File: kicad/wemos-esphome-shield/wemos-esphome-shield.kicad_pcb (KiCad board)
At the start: 2 copper layers, 74 x 54 mm, 13 parts, among them Q1 2N2219, T1 Transformer_1P_1S, U1 WeMos_D1_mini

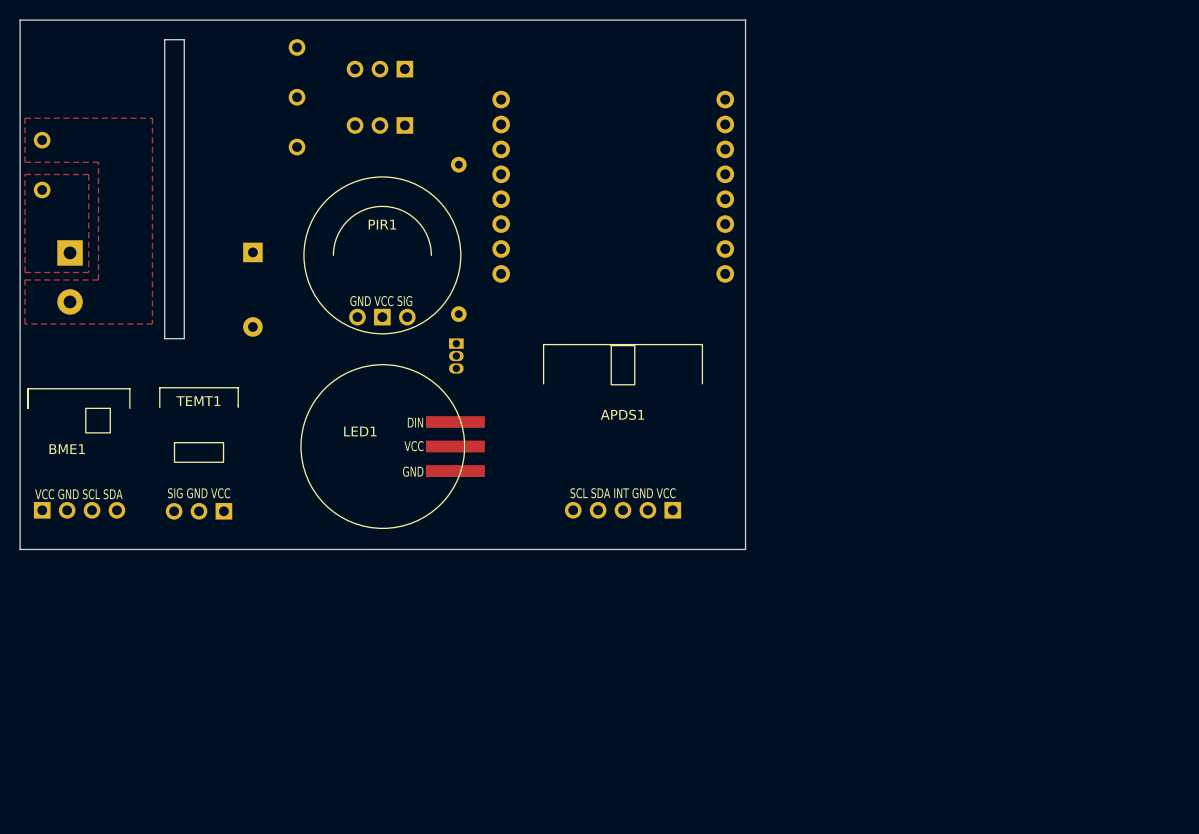
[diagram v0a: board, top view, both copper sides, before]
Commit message: Fix some electrical net, new cut edge, new netclasses
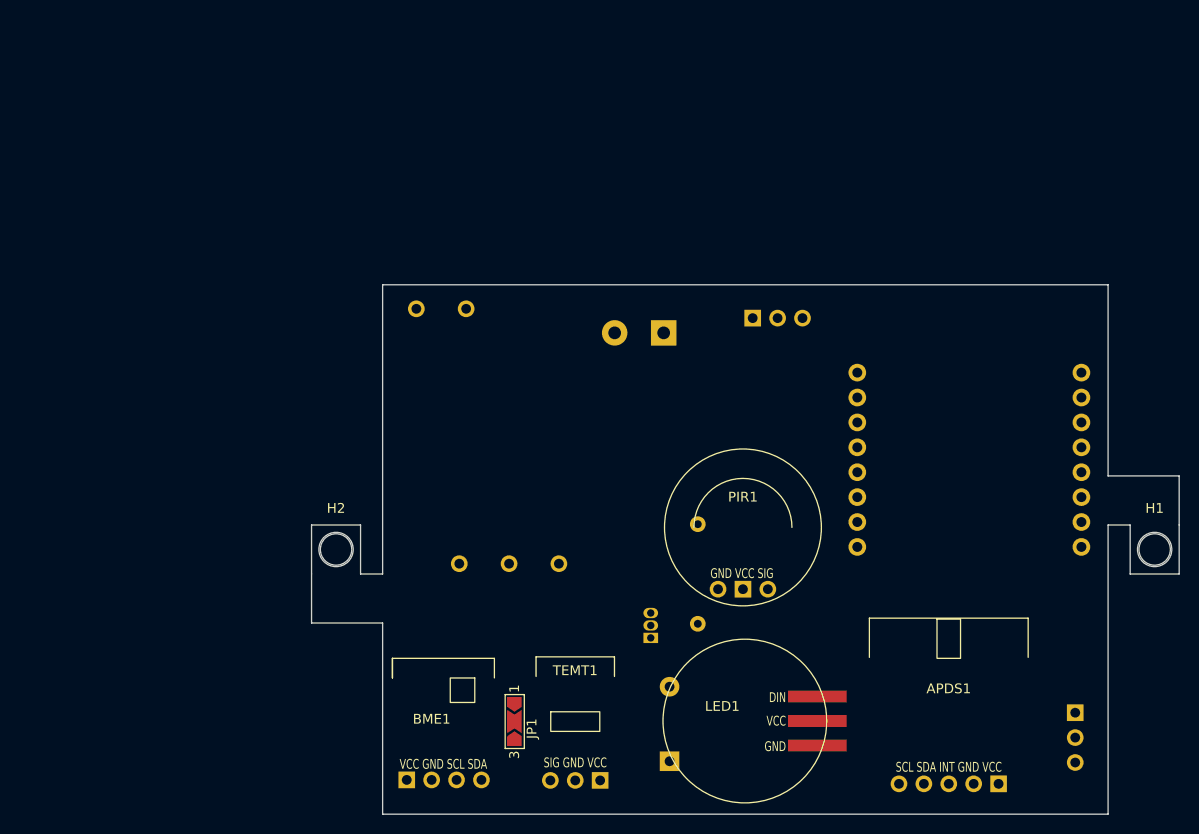
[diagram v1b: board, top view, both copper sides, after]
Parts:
- added H1: MountingHole, MountingHole:MountingHole_3.2mm_M3, F.Cu at (157.7, 91.0)
- added H2: MountingHole, MountingHole:MountingHole_3.2mm_M3, F.Cu at (74.2, 91.0)
- added JP1: SolderJumper_3_Open, Jumper:SolderJumper-3_P2.0mm_Open_TrianglePad1.0x1.5mm_NumberLabels, F.Cu at (92.4, 108.5)
- APDS1: value Conn_01x04_Female -> Conn_01x05_Female
- R1: footprint Resistor_THT:R_Axial_DIN0207_L6.3mm_D2.5mm_P15.24mm_Horizontal -> Resistor_THT:R_Axial_DIN0207_L6.3mm_D2.5mm_P10.16mm_Horizontal
- moved RELAY1 94.8 mm to (149.6, 107.7), turned to 180 degrees
- moved BZ1 67.1 mm to (108.2, 112.6), turned to 90 degrees
- moved POWER1 61.1 mm to (107.7, 68.9), turned to 180 degrees
- moved TEMT1 47.2 mm to (98.6, 114.6)
- moved LED1 46.3 mm to (115.9, 108.5)
- moved BME1 46.2 mm to (84.0, 114.5)
- moved PIR1 46.1 mm to (115.7, 95.0)
- moved U1 45.8 mm to (138.8, 81.8)
- moved T1 45.6 mm to (89.5, 79.5), turned to -90 degrees
- moved R1 44.0 mm to (111.1, 88.4)
- moved APDS1 43.4 mm to (136.7, 114.9)
- moved RELAY2 40.6 mm to (116.7, 67.4), turned to -90 degrees
- moved Q1 36.0 mm to (106.3, 100.0), turned to 90 degrees
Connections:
- APDS1 pad 1: SDA -> SCL
- APDS1 pad 2: SCL -> SDA
- APDS1 pad 3: 5V -> unconnected-(APDS1-Pad3)
- APDS1 pad 5: (no net) -> 5V
- BME1 pad 1: SDA -> Net-(JP1-Pad2)
- BME1 pad 2: SCL -> GND
- BME1 pad 3: 5V -> SCL
- BME1 pad 4: GND -> SDA
- PIR1 pad 1: 3.3V -> GND
- PIR1 pad 2: GND -> 3.3V
- TEMT1 pad 1: 5V -> TEMT6000
- TEMT1 pad 2: TEMT6000 -> GND
- TEMT1 pad 3: GND -> 5V
- U1 pad 9: 5V -> VCC
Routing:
- removed copper zone on F.Cu, net L
- removed copper zone on F.Cu, net N
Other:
- board size 74 x 54 mm -> 88.5 x 54 mm

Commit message: first routing version
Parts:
- moved RELAY2 49.8 mm to (144.9, 108.4), turned to 0 degrees
- moved Q1 19.0 mm to (105.8, 81.0)
- moved BZ1 14.3 mm to (106.2, 98.5)
- moved R1 13.7 mm to (102.3, 78.0)
- moved LED1 7.05 mm to (115.8, 101.5), turned to -90 degrees
- moved JP1 6.43 mm to (93.5, 102.2)
- moved TEMT1 6.27 mm to (99.5, 108.4)
- moved APDS1 6.22 mm to (134.8, 109.0)
- moved BME1 6.15 mm to (84.8, 108.4)
- moved PIR1 4.31 mm to (116.0, 90.8)
- moved U1 2.34 mm to (136.6, 81.2)
- moved RELAY1 0.81 mm to (150.0, 108.4), turned to 0 degrees
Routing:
- net GND: track 0.00 -> 189.2 mm
- net 3.3V: track 0.00 -> 99.1 mm
- net SCL: track 0.00 -> 79.0 mm
- net TEMT6000: track 0.00 -> 76.6 mm
- net SDA: track 0.00 -> 74.1 mm, vias 0 -> 1
- net 5V: track 0.00 -> 72.8 mm
- net LED: track 0.00 -> 52.3 mm, vias 0 -> 1
- net VCC: track 0.00 -> 38.8 mm
- net L: track 0.00 -> 30.2 mm
- net RELAY1: track 0.00 -> 28.8 mm
- net BUZZER: track 0.00 -> 25.7 mm
- net RELAY2: track 0.00 -> 24.7 mm
- net Net-(BZ1-Pad2): track 0.33 -> 19.4 mm
- net N: track 0.00 -> 16.2 mm
- net Net-(JP1-Pad2): track 0.14 -> 16.3 mm
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
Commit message: update APDS footprint for future compatibility
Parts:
- APDS1: footprint internal:APDS9960 -> internal:APDS9960 double pinout
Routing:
- net SCL: track 79.0 -> 91.8 mm
- net SDA: track 74.1 -> 82.0 mm
- net GND: track 189.2 -> 192.3 mm
- net 5V: track 72.8 -> 75.8 mm
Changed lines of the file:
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@@
   (net 21 "RELAY2")
   (net 22 "unconnected-(APDS1-Pad3)")
-  (net 23 "Net-(JP1-Pad2)")
+  (net 23 "Net-(BME1-Pad1)")
   (footprint "internal:SR602" locked (layer "F.Cu")
     (at 115.954688 90.75)
@@
       (net 1 "5V") (pinfunction "Pin_3") (pintype "passive"))
   )
-  (footprint "internal:APDS9960" (layer "F.Cu")
+  (footprint "internal:APDS9960 double pinout" (layer "F.Cu")
     (at 134.75 109.005)
     (property "Sheetfile" "wemos-esphome-shield.kicad_sch")
@@
       (effects (font (size 1 1) (thickness 0.15)))
     )
-    (fp_text user "SCL SDA INT GND VCC" (at 0 -1.7 unlocked) (layer "F.SilkS")
+    (fp_text user "GND VCC SDA SCL" (at 0 3.8 unlocked) (layer "F.SilkS")
+      (effects (font (size 1 0.7) (thickness 0.15)))
+    )
+    (fp_text user "SCL SDA INT GND VCC" (at 0 -1.6 unlocked) (layer "F.SilkS")
       (effects (font (size 1 0.7) (thickness 0.15)))
     )
@@
     (fp_line (start 8.1 -16.9) (end 8.1 -12.9) (layer "F.SilkS") (width 0.12))
     (fp_line (start -8.1 -16.9) (end -8.1 -12.9) (layer "F.SilkS") (width 0.12))
-    (fp_line (start -8.1 -16.9) (end 8.1 -16.9) (layer "F.SilkS") (width 0.12))
     (fp_rect (start -1.2 -16.8) (end 1.2 -12.8) (layer "F.SilkS") (width 0.12) (fill none))
-    (fp_rect (start -8.1 1.1) (end 8.1 -16.9) (layer "F.Fab") (width 0.1) (fill none))
+    (fp_rect (start -8.1 -17.2) (end 8.1 3.2) (layer "F.Fab") (width 0.1) (fill none))
+    (pad "1" thru_hole circle (at 3.81 2.1) (size 1.7 1.7) (drill 1) (layers *.Cu *.Mask)
+      (net 4 "SCL") (pinfunction "Pin_1") (pintype "passive"))
     (pad "1" thru_hole circle (at -5.08 0) (size 1.7 1.7) (drill 1) (layers *.Cu *.Mask)
       (net 4 "SCL") (pinfunction "Pin_1") (pintype "passive"))
     (pad "2" thru_hole circle (at -2.54 0) (size 1.7 1.7) (drill 1) (layers *.Cu *.Mask)
       (net 2 "SDA") (pinfunction "Pin_2") (pintype "passive"))
+    (pad "2" thru_hole circle (at 1.27 2.1) (size 1.7 1.7) (drill 1) (layers *.Cu *.Mask)
+      (net 2 "SDA") (pinfunction "Pin_2") (pintype "passive"))
     (pad "3" thru_hole circle (at 0 0) (size 1.7 1.7) (drill 1) (layers *.Cu *.Mask)
       (net 22 "unconnected-(APDS1-Pad3)") (pinfunction "Pin_3") (pintype "passive+no_connect"))
+    (pad "4" thru_hole circle (at -3.81 2.1) (size 1.7 1.7) (drill 1) (layers *.Cu *.Mask)
+      (net 8 "GND") (pinfunction "Pin_4") (pintype "passive"))
     (pad "4" thru_hole circle (at 2.54 0) (size 1.7 1.7) (drill 1) (layers *.Cu *.Mask)
       (net 8 "GND") (pinfunction "Pin_4") (pintype "passive"))
     (pad "5" thru_hole rect (at 5.08 0) (size 1.7 1.7) (drill 1) (layers *.Cu *.Mask)
+      (net 1 "5V") (pinfunction "Pin_5") (pintype "passive"))
+    (pad "5" thru_hole rect (at -1.27 2.1) (size 1.7 1.7) (drill 1) (layers *.Cu *.Mask)
       (net 1 "5V") (pinfunction "Pin_5") (pintype "passive"))
   )
@@
       ))
     (pad "2" smd custom (at 0 0 270) (size 0.3 0.3) (layers "F.Cu")
-      (net 23 "Net-(JP1-Pad2)") (pinfunction "C") (pintype "passive") (zone_connect 2)
+      (net 23 "Net-(BME1-Pad1)") (pinfunction "C") (pintype "passive") (zone_connect 2)
       (options (clearance outline) (anchor rect))
       (primitives
@@
     (fp_rect (start -4 1.4) (end 6.4 -12.4) (layer "F.Fab") (width 0.1) (fill none))
     (pad "1" thru_hole rect (at -2.54 0) (size 1.7 1.7) (drill 1) (layers *.Cu *.Mask)
-      (net 23 "Net-(JP1-Pad2)") (pinfunction "Pin_1") (pintype "passive"))
+      (net 23 "Net-(BME1-Pad1)") (pinfunction "Pin_1") (pintype "passive"))
     (pad "2" thru_hole circle (at 0 0) (size 1.7 1.7) (drill 1) (layers *.Cu *.Mask)
       (net 8 "GND") (pinfunction "Pin_2") (pintype "passive"))
@@
   (segment (start 118.15 113.55) (end 115.85 111.25) (width 0.25) (layer "F.Cu") (net 1))
   (segment (start 139.83 109.005) (end 139.83 110.77) (width 0.25) (layer "F.Cu") (net 1))
+  (segment (start 137.05 113.55) (end 134.7 113.55) (width 0.25) (layer "F.Cu") (net 1))
   (segment (start 139.83 109.005) (end 144.32 109.005) (width 0.25) (layer "F.Cu") (net 1))
   (segment (start 115.85 104.25) (end 115.9 104.2) (width 0.25) (layer "F.Cu") (net 1))
-  (segment (start 137.05 113.55) (end 118.15 113.55) (width 0.25) (layer "F.Cu") (net 1))
   (segment (start 115.85 108.85) (end 115.85 104.25) (width 0.25) (layer "F.Cu") (net 1))
+  (segment (start 133.48 112.33) (end 134.7 113.55) (width 0.25) (layer "F.Cu") (net 1))
+  (segment (start 133.48 111.105) (end 133.48 112.33) (width 0.25) (layer "F.Cu") (net 1))
   (segment (start 100.6 104.2) (end 93.45 104.2) (width 0.25) (layer "F.Cu") (net 1))
   (segment (start 150 108.375) (end 144.95 108.375) (width 0.25) (layer "F.Cu") (net 1))
@@
   (segment (start 144.32 109.005) (end 144.95 108.375) (width 0.25) (layer "F.Cu") (net 1))
   (segment (start 105.395 108.355) (end 109.55 104.2) (width 0.25) (layer "F.Cu") (net 1))
+  (segment (start 134.7 113.55) (end 118.15 113.55) (width 0.25) (layer "F.Cu") (net 1))
   (segment (start 102.09 105.69) (end 100.6 104.2) (width 0.25) (layer "F.Cu") (net 1))
   (segment (start 125.17 79.88) (end 127.55 82.26) (width 0.25) (layer "F.Cu") (net 2))
   (segment (start 127.55 82.26) (end 127.55 106.75) (width 0.25) (layer "F.Cu") (net 2))
   (via (at 127.55 106.75) (size 0.8) (drill 0.4) (layers "F.Cu" "B.Cu") (net 2))
+  (segment (start 134.9 106.9) (end 131.65 106.9) (width 0.25) (layer "B.Cu") (net 2))
   (segment (start 91.655 110.18) (end 124.17 110.18) (width 0.25) (layer "B.Cu") (net 2))
   (segment (start 127.45 106.9) (end 131.65 106.9) (width 0.25) (layer "B.Cu") (net 2))
+  (segment (start 136.02 108.02) (end 134.9 106.9) (width 0.25) (layer "B.Cu") (net 2))
   (segment (start 89.88 108.405) (end 91.655 110.18) (width 0.25) (layer "B.Cu") (net 2))
   (segment (start 132.21 107.46) (end 132.21 109.005) (width 0.25) (layer "B.Cu") (net 2))
   (segment (start 124.17 110.18) (end 127.45 106.9) (width 0.25) (layer "B.Cu") (net 2))
   (segment (start 131.65 106.9) (end 132.21 107.46) (width 0.25) (layer "B.Cu") (net 2))
-  (segment (start 129.67 81.84) (end 129.67 109.005) (width 0.25) (layer "F.Cu") (net 4))
+  (segment (start 136.02 111.105) (end 136.02 108.02) (width 0.25) (layer "B.Cu") (net 2))
+  (segment (start 135.83 105.58) (end 129.67 105.58) (width 0.25) (layer "F.Cu") (net 4))
+  (segment (start 138.56 108.31) (end 135.83 105.58) (width 0.25) (layer "F.Cu") (net 4))
+  (segment (start 129.67 105.58) (end 129.67 109.005) (width 0.25) (layer "F.Cu") (net 4))
+  (segment (start 129.67 81.84) (end 129.67 105.58) (width 0.25) (layer "F.Cu") (net 4))
+  (segment (start 138.56 111.105) (end 138.56 108.31) (width 0.25) (layer "F.Cu") (net 4))
   (segment (start 125.17 77.34) (end 129.67 81.84) (width 0.25) (layer "F.Cu") (net 4))
   (segment (start 127.125 111.55) (end 89.2 111.55) (width 0.25) (layer "B.Cu") (net 4))
@@
   (segment (start 104.65 85.65) (end 105.85 84.45) (width 0.25) (layer "F.Cu") (net 8))
   (segment (start 113.3 112.2) (end 113.4 112.1) (width 0.25) (layer "F.Cu") (net 8))
+  (segment (start 130.94 112.69) (end 132 113.75) (width 0.25) (layer "B.Cu") (net 8))
   (segment (start 137.29 104.84) (end 137.25 104.8) (width 0.25) (layer "B.Cu") (net 8))
+  (segment (start 86.6 113.75) (end 132 113.75) (width 0.25) (layer "B.Cu") (net 8))
   (segment (start 138.755 103.295) (end 137.25 104.8) (width 0.25) (layer "B.Cu") (net 8))
-  (segment (start 86.6 113.75) (end 135.3 113.75) (width 0.25) (layer "B.Cu") (net 8))
   (segment (start 135.3 113.75) (end 137.29 111.76) (width 0.25) (layer "B.Cu") (net 8))
   (segment (start 113.414688 87.335312) (end 113.414688 90.75) (width 0.25) (layer "B.Cu") (net 8))
   (segment (start 125.17 87.5) (end 113.579376 87.5) (width 0.25) (layer "B.Cu") (net 8))
   (segment (start 137.29 109.005) (end 137.29 104.84) (width 0.25) (layer "B.Cu") (net 8))
+  (segment (start 130.94 111.105) (end 130.94 112.69) (width 0.25) (layer "B.Cu") (net 8))
   (segment (start 86.8 92.45) (end 84.8 94.45) (width 0.25) (layer "B.Cu") (net 8))
   (segment (start 84.8 111.95) (end 86.6 113.75) (width 0.25) (layer "B.Cu") (net 8))
@@
   (segment (start 84.8 108.405) (end 84.8 111.95) (width 0.25) (layer "B.Cu") (net 8))
   (segment (start 84.8 94.45) (end 84.8 108.405) (width 0.25) (layer "B.Cu") (net 8))
+  (segment (start 132 113.75) (end 135.3 113.75) (width 0.25) (layer "B.Cu") (net 8))
   (segment (start 105.85 81.05) (end 110.3 81.05) (width 0.25) (layer "B.Cu") (net 8))
   (segment (start 113.414688 84.164688) (end 113.414688 87.335312) (width 0.25) (layer "B.Cu") (net 8))

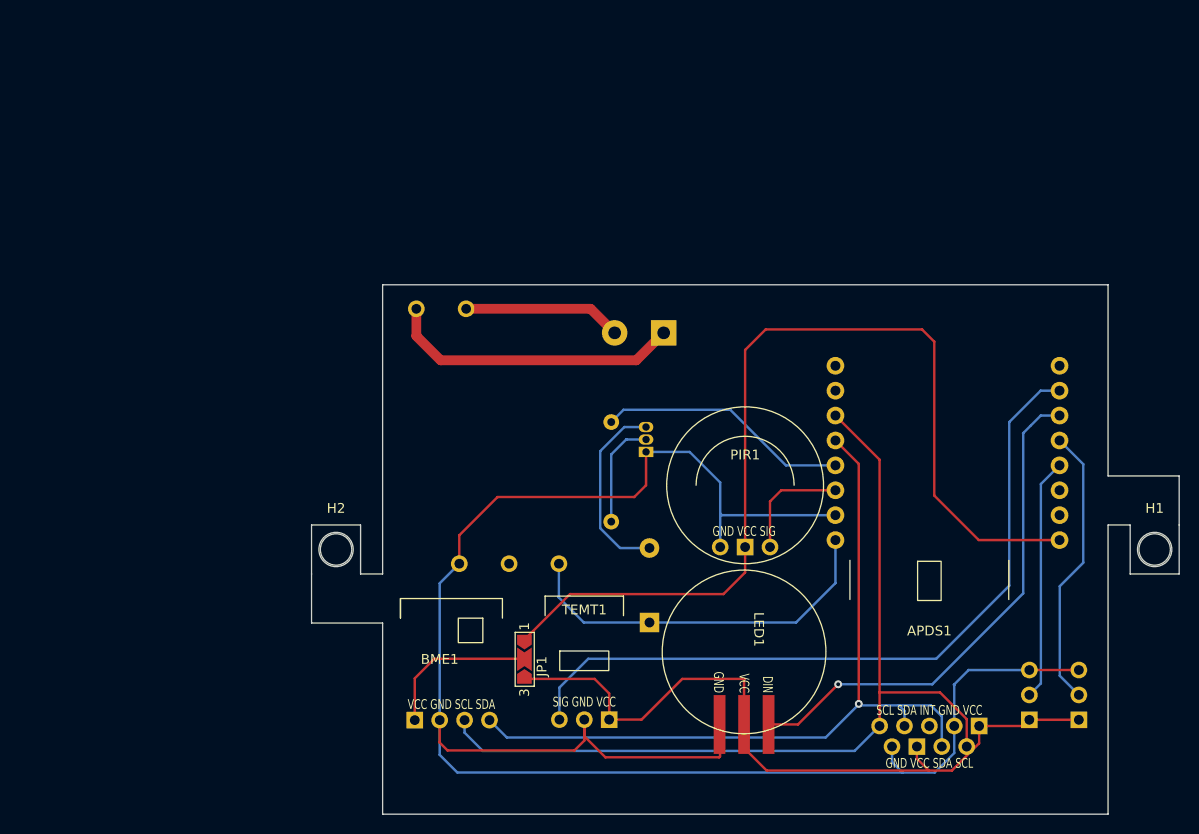
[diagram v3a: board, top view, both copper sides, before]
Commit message: transistor driven relay pin, expose more extra pins, and routing
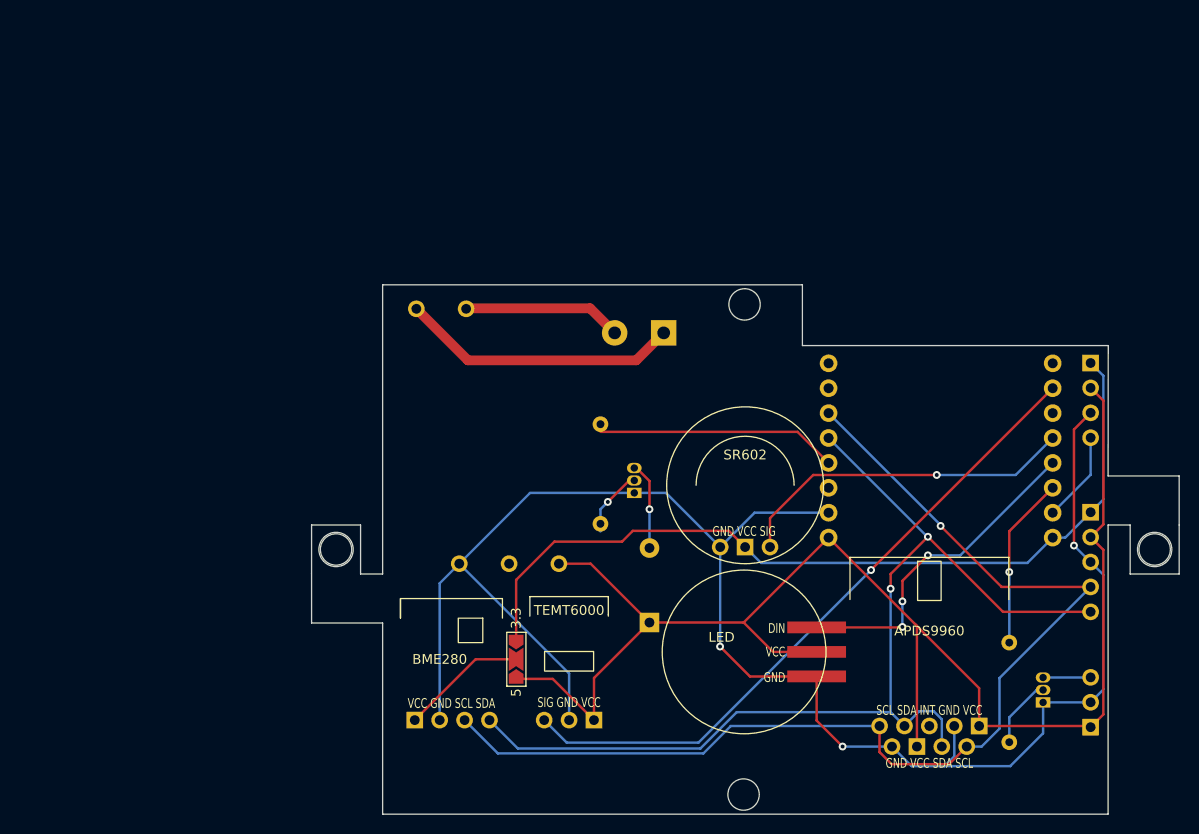
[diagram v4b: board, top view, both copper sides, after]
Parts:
- removed RELAY2: Conn_01x03_Female, Connector_PinHeader_2.54mm:PinHeader_1x03_P2.54mm_Vertical
- added H3: MountingHole, MountingHole:MountingHole_3.2mm_M3, F.Cu at (115.9, 66.0)
- added H4: MountingHole, MountingHole:MountingHole_3.2mm_M3, F.Cu at (115.8, 116.0)
- added PIN1: Conn_01x05_Female, Connector_PinHeader_2.54mm:PinHeader_1x05_P2.54mm_Vertical, B.Cu at (151.2, 87.2)
- added PIN2: Conn_01x04_Female, Connector_PinHeader_2.54mm:PinHeader_1x04_P2.54mm_Vertical, B.Cu at (151.2, 72.0)
- added Q2: 2N2219, Package_TO_SOT_THT:TO-92L_Inline, B.Cu at (146.3, 106.6)
- added R2: R_Small, Resistor_THT:R_Axial_DIN0207_L6.3mm_D2.5mm_P10.16mm_Horizontal, B.Cu at (142.9, 100.5)
- moved Q1 4.35 mm to (104.7, 85.2)
- moved TEMT6000 1.55 mm to (98.0, 108.4)
- moved RELAY1 1.42 mm to (151.2, 109.1)
- moved R1 1.12 mm to (101.2, 78.2)
- moved JP1 0.85 mm to (92.6, 102.2)
- moved U1 0.74 mm to (135.9, 80.9)
- turned LED to 0 degrees
- renumbered APDS1 to APDS9960, BME1 to BME280, LED1 to LED, PIR1 to SR602, TEMT1 to TEMT6000
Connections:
- net BUZZER renamed D3
- net TEMT6000 renamed A0
- BZ1 pad 1: VCC -> 5V
- LED pad 1: LED -> D6
- RELAY1 pad 2: RELAY1 -> GND
- RELAY1 pad 3: GND -> Net-(Q2-Pad3)
- SR602 pad 3: PIR -> D5
- T1 pad 4: VCC -> 5V
- U1 pad 11: PIR -> unconnected-(U1-Pad11)
- U1 pad 3: LED -> unconnected-(U1-Pad3)
- U1 pad 4: RELAY1 -> D5
- U1 pad 5: RELAY2 -> D6
- U1 pad 6: unconnected-(U1-Pad6) -> D7
- U1 pad 7: unconnected-(U1-Pad7) -> D8
- U1 pad 9: VCC -> 5V
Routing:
- net 5V: track 75.8 -> 150.6 mm
- net LED: track 52.3 -> 0.00 mm, vias 1 -> 0
- net VCC: track 38.8 -> 0.00 mm
- net D5: track 0.00 -> 35.2 mm, vias 0 -> 1
- net D6: track 0.00 -> 33.8 mm, vias 0 -> 3
- net RELAY1: track 28.8 -> 0.00 mm
- net SDA: track 82.0 -> 106.8 mm, vias 1 -> 2
- net RELAY2: track 24.7 -> 0.00 mm
- net SCL: track 91.8 -> 114.2 mm, vias 0 -> 1
- net D7: track 0.00 -> 17.5 mm, vias 0 -> 1
- net GND: track 192.3 -> 178.5 mm, vias 0 -> 3
- net 3.3V: track 99.1 -> 86.6 mm
- net PIR: track 11.8 -> 0.00 mm
- net Net-(BZ1-Pad2): track 19.4 -> 8.93 mm, vias 0 -> 1
- net D8: track 0.00 -> 9.25 mm
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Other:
- outline, holes or cut-outs redrawn
- board text added: "3.3 5v GND D8"
- board text added: "3.3 5v GND SCL SDA"
- board text added: "D5 VCC GND"
- board text added: "RELAY"
- board text added: "SCL SDA VCC GND"
- board text added: "SDA SCL GND VCC"
- board text added: "SIG GND 5V"
- board text added: "VCC GND SIG"
